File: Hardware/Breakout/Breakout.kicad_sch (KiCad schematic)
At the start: 1 part, among them IC1 NUCLEO-G431KB

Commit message: Added few parts
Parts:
- added U1: TDC7200PWR, SOP65P640X120-14N, symbol TDC7200PWR:TDC7200PWR
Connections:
- net GND1: now also U1.7 (GND)
- net at IC1.13 (PA11(D10)): now also U1.11 (~{CS})
- net at IC1.14 (PB5(D11)): now also U1.9 (DOUT)
- net at IC1.15 (PB4(D12)): now also U1.10 (DIN)
- net at IC1.16 (PB3(D13)): now also U1.12 (SCLK)
- net at IC1.17 (+3V3): now also U1.14 (VDD)
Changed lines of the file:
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@@
+    (stroke (width 0) (type default))
+  )
+  (wire (pts (xy 66.04 101.6) (xy 66.04 116.84))
+    (stroke (width 0) (type default))
+  )
+  (wire (pts (xy 116.84 106.68) (xy 134.62 106.68))
+    (stroke (width 0) (type default))
+  )
+  (wire (pts (xy 147.32 116.84) (xy 147.32 106.68))
+    (stroke (width 0) (type default))
+  )
+  (wire (pts (xy 134.62 109.22) (xy 163.83 109.22))
+    (stroke (width 0) (type default))
+  )
+  (wire (pts (xy 134.62 106.68) (xy 134.62 109.22))
     (stroke (width 0) (type default))
   )
@@
     (stroke (width 0) (type default))
   )
+  (wire (pts (xy 68.58 104.14) (xy 68.58 114.3))
+    (stroke (width 0) (type default))
+  )
+  (wire (pts (xy 68.58 114.3) (xy 163.83 114.3))
+    (stroke (width 0) (type default))
+  )
   (wire (pts (xy 116.84 71.12) (xy 121.92 71.12))
     (stroke (width 0) (type default))
   )
+  (wire (pts (xy 71.12 101.6) (xy 66.04 101.6))
+    (stroke (width 0) (type default))
+  )
+  (wire (pts (xy 147.32 106.68) (xy 163.83 106.68))
+    (stroke (width 0) (type default))
+  )
+  (wire (pts (xy 139.7 86.36) (xy 163.83 86.36))
+    (stroke (width 0) (type default))
+  )
+  (wire (pts (xy 71.12 111.76) (xy 163.83 111.76))
+    (stroke (width 0) (type default))
+  )
+  (wire (pts (xy 116.84 104.14) (xy 139.7 104.14))
+    (stroke (width 0) (type default))
+  )
+  (wire (pts (xy 139.7 104.14) (xy 139.7 86.36))
+    (stroke (width 0) (type default))
+  )
+  (wire (pts (xy 66.04 116.84) (xy 147.32 116.84))
+    (stroke (width 0) (type default))
+  )
+  (wire (pts (xy 71.12 106.68) (xy 71.12 111.76))
+    (stroke (width 0) (type default))
+  )
   (wire (pts (xy 127 73.66) (xy 116.84 73.66))
     (stroke (width 0) (type default))
   )
+  (wire (pts (xy 199.39 121.92) (xy 203.2 121.92))
+    (stroke (width 0) (type default))
+  )
+  (wire (pts (xy 203.2 121.92) (xy 203.2 127))
+    (stroke (width 0) (type default))
+  )
+  (wire (pts (xy 71.12 104.14) (xy 68.58 104.14))
+    (stroke (width 0) (type default))
+  )
   (symbol (lib_id "power:GND1") (at 127 63.5 180) (unit 1)
     (in_bom yes) (on_board yes) (dnp no) (fields_autoplaced)
@@
         (path "/c2ef38f9-0f55-4b19-9130-d81b036a0cd1"
           (reference "#PWR01") (unit 1)
+        )
+      )
+    )
+  )
+  (symbol (lib_id "power:GND1") (at 203.2 127 0) (unit 1)
+    (in_bom yes) (on_board yes) (dnp no) (fields_autoplaced)
+    (property "Reference" "#PWR03" (at 203.2 133.35 0)
+      (effects (font (size 1.27 1.27)) hide)
+    )
+    (property "Value" "GND1" (at 203.2 132.08 0)
+      (effects (font (size 1.27 1.27)))
+    )
+    (property "Footprint" "" (at 203.2 127 0)
+      (effects (font (size 1.27 1.27)) hide)
+    )
+    (property "Datasheet" "" (at 203.2 127 0)
+      (effects (font (size 1.27 1.27)) hide)
+    )
+    (pin "1")
+    (instances
+      (project "Breakout"
+        (path "/c2ef38f9-0f55-4b19-9130-d81b036a0cd1"
+          (reference "#PWR03") (unit 1)
         )
       )
@@
         )
       )
+    )
+  )
+  (symbol (lib_id "TDC7200PWR:TDC7200PWR") (at 181.61 104.14 0) (unit 1)
+    (in_bom yes) (on_board yes) (dnp no) (fields_autoplaced)
+    (property "Reference" "U1" (at 181.61 78.74 0)
+      (effects (font (size 1.27 1.27)))
+    )
+    (property "Value" "TDC7200PWR" (at 181.61 81.28 0)
+      (effects (font (size 1.27 1.27)))
+    )
+    (property "Footprint" "SOP65P640X120-14N" (at 181.61 104.14 0)
+      (effects (font (size 1.27 1.27)) (justify bottom) hide)
+    )
+    (property "Datasheet" "" (at 181.61 104.14 0)
+      (effects (font (size 1.27 1.27)) hide)
+    )
+    (property "PARTREV" "D" (at 181.61 104.14 0)
+      (effects (font (size 1.27 1.27)) (justify bottom) hide)
+    )
+    (property "MANUFACTURER" "Texas Instruments" (at 181.61 104.14 0)
+      (effects (font (size 1.27 1.27)) (justify bottom) hide)
+    )
+    (property "MAXIMUM_PACKAGE_HEIGHT" "1.2 mm" (at 181.61 104.14 0)
+      (effects (font (size 1.27 1.27)) (justify bottom) hide)
+    )
+    (property "STANDARD" "IPC 7351B" (at 181.61 104.14 0)
+      (effects (font (size 1.27 1.27)) (justify bottom) hide)
+    )
+    (pin "1")
+    (pin "10")
+    (pin "11")
+    (pin "12")
+    (pin "13")
+    (pin "14")
+    (pin "2")
+    (pin "3")
+    (pin "4")
+    (pin "5")
+    (pin "6")
+    (pin "7")
+    (pin "8")
+    (pin "9")
+    (instances
+      (project "Breakout"
+        (path "/c2ef38f9-0f55-4b19-9130-d81b036a0cd1"
+          (reference "U1") (unit 1)
+        )
+      )

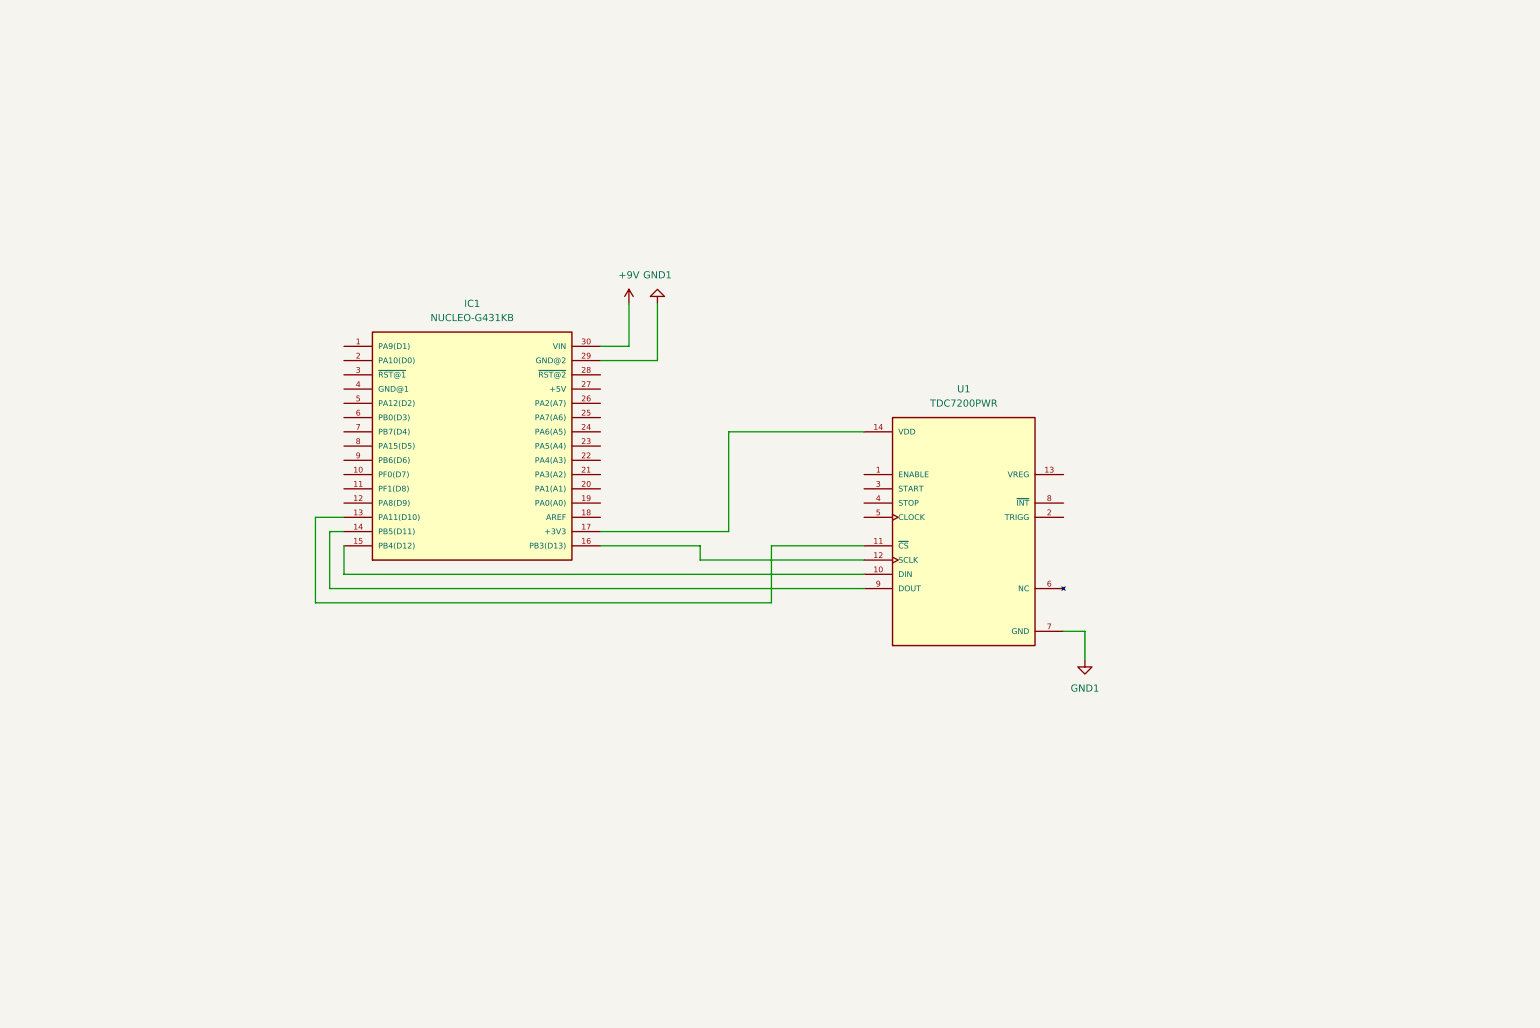
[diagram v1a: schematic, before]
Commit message: Added TDC circiut to main schem, still need to make sure its all hoodked up right
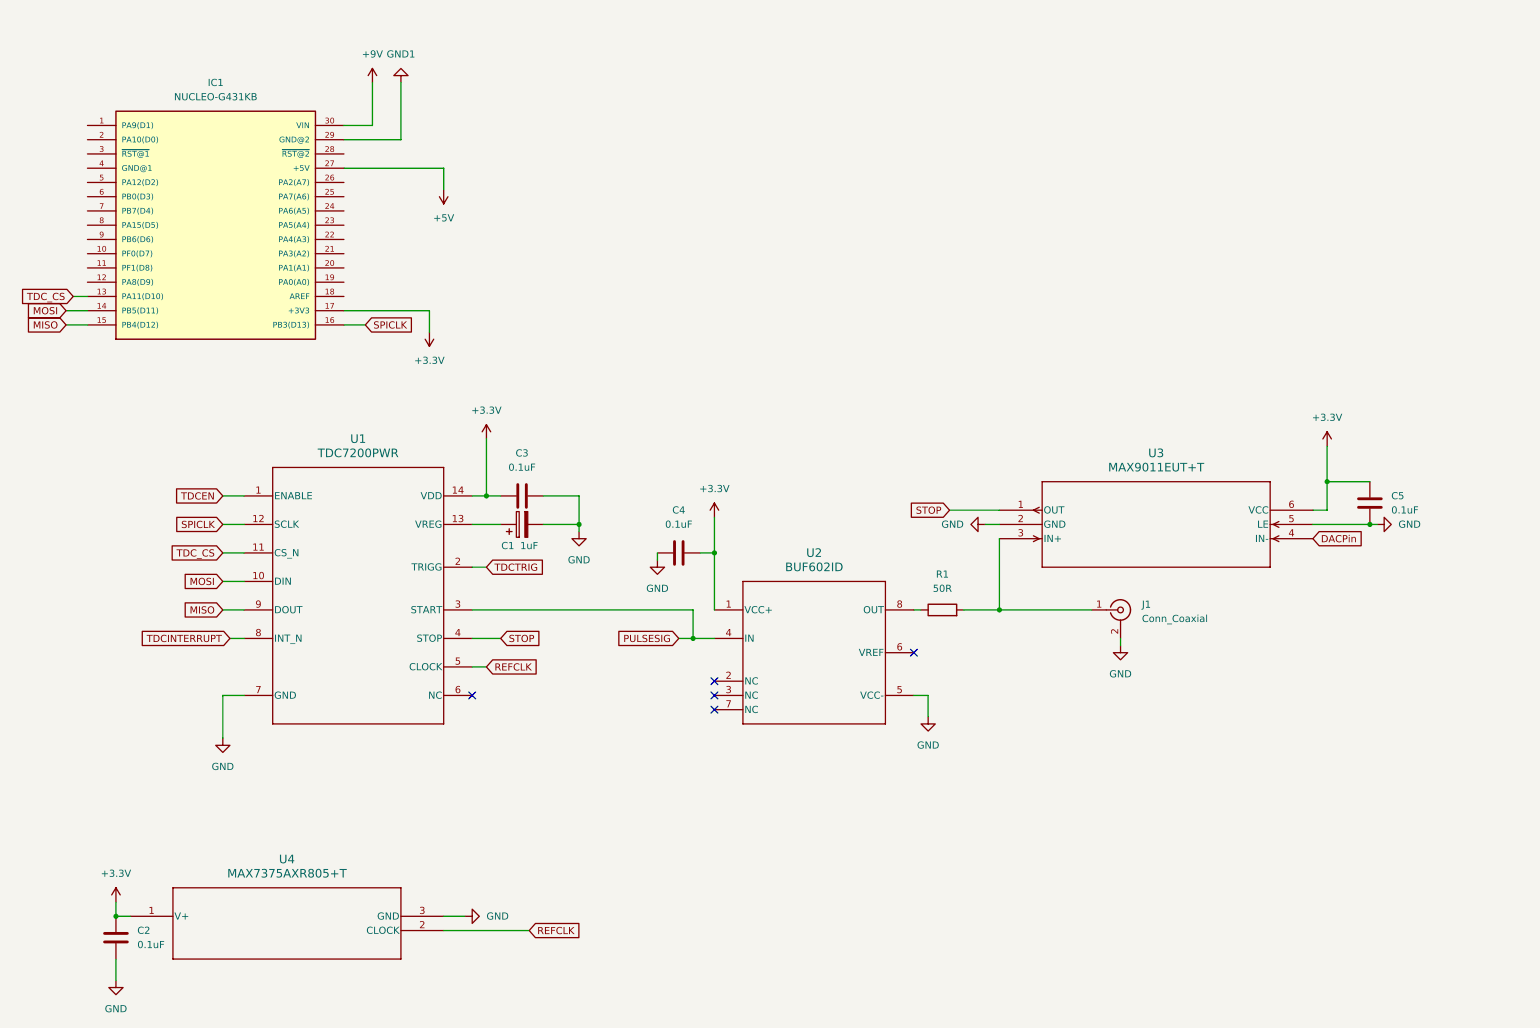
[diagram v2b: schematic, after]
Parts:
- removed U1: TDC7200PWR, SOP65P640X120-14N, symbol TDC7200PWR:TDC7200PWR
- added C1: 1uF, symbol Device:C_Polarized
- added C2, C3, C4, C5: 0.1uF, symbol Device:C
- added J1: Conn_Coaxial, symbol Connector:Conn_Coaxial
- added R1: 50R, symbol Device:R
- added U1: TDC7200PWR, PW0014A_N, symbol TDC:TDC7200PWR
- added U2: BUF602ID, D0008A_N, symbol 2023-07-05_03-38-51:BUF602ID
- added U3: MAX9011EUT+T, 21-0058I_MXM, symbol 2023-07-05_03-30-52:MAX9011EUT+T
- added U4: MAX7375AXR805+T, 21-0075D_MXM, symbol 2023-07-05_04-24-47:MAX7375AXR805+T
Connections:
- net TDC_CS: now reaches IC1.13 (PA11(D10))
- net TDC_CS: now also U1.11 (CS_N)
- net MOSI: now reaches IC1.14 (PB5(D11))
- net MOSI: now also U1.10 (DIN)
- net MISO: now reaches IC1.15 (PB4(D12))
- net MISO: now also U1.9 (DOUT)
- net SPICLK: now reaches IC1.16 (PB3(D13))
- net SPICLK: now also U1.12 (SCLK)
- net +3.3V: now reaches IC1.17 (+3V3)
- net +3.3V: now also C2.1, C3.1, C4.2, C5.2, U1.14 (VDD), U2.1 (VCC+), U3.6 (VCC), U4.1 (V+)
- net +5V: now reaches IC1.27 (+5V)
- new net: J1.1 (In), R1.2, U3.3 (IN+)
- new net: R1.1, U2.8 (OUT)
- new net: C1.1, U1.13 (VREG)
- new net DACPin: U3.4 (IN-)
- new net GND: C1.2, C2.2, C3.2, C4.1, C5.1, J1.2 (Ext), U1.7 (GND), U2.5 (VCC-), U3.2 (GND), U3.5 (LE), U4.3 (GND)
- new net PULSESIG: U1.3 (START), U2.4 (IN)
- new net REFCLK: U1.5 (CLOCK), U4.2 (CLOCK)
- new net STOP: U1.4 (STOP), U3.1 (OUT)
- new net TDCEN: U1.1 (ENABLE)
- new net TDCINTERRUPT: U1.8 (INT_N)
- new net TDCTRIG: U1.2 (TRIGG)
- no-connect marks 0 -> 5
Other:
- moved on the sheet: IC1

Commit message: Upload of hardware changes as of 6pm 06/07/2023
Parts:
- added B2: SSD1306, Library:Adafruit_SSD1306_4Pin, symbol SSD1306-128x64_OLED:SSD1306
- B1: renamed from IC1; footprint (none) -> NUCLEO-G431KB:DIPS1524W66P254L5029H1500Q30N
- C1: footprint (none) -> UWT1HH010MCL1GB:PCAP_4x5.4-ELECT_NCA-L
- C2, C3, C4, C5: footprint (none) -> 06035C104JAT2A:CAPC1608X90N
- J1: footprint (none) -> Library:0731375003_BCN_conn
- U1: footprint PW0014A_N -> TDC7200PWR:SOP65P640X120-14N
- U2: footprint D0008A_N -> BUF602ID:D0008A_N
- U3: footprint 21-0058I_MXM -> MAX9011EUT:21-0058I_MXM
- U4: footprint 21-0075D_MXM -> MAX737AXR805:21-0075D_MXM
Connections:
- net GND1 is gone; now on net GND: B1.29 (GND@2)
- net +3.3V: now also B2.2 (VCC)
- net DACPin: now also B1.26 (PA2(A7))
- net GND: now also B1.4 (GND@1), B2.1 (GND)
- net PULSESIG: now also B1.6 (PB0(D3))
- net TDCEN: now also B1.9 (PB6(D6))
- net TDCINTERRUPT: now also B1.12 (PA8(D9))
- net TDCTRIG: now also B1.10 (PF0(D7))
- net SDA: now reaches B1.7 (PB7(D4))
- net SDA: now also B2.4 (SDA)
- net SCL: now reaches B1.8 (PA15(D5))
- net SCL: now also B2.3 (SCL)
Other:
- moved on the sheet: B1

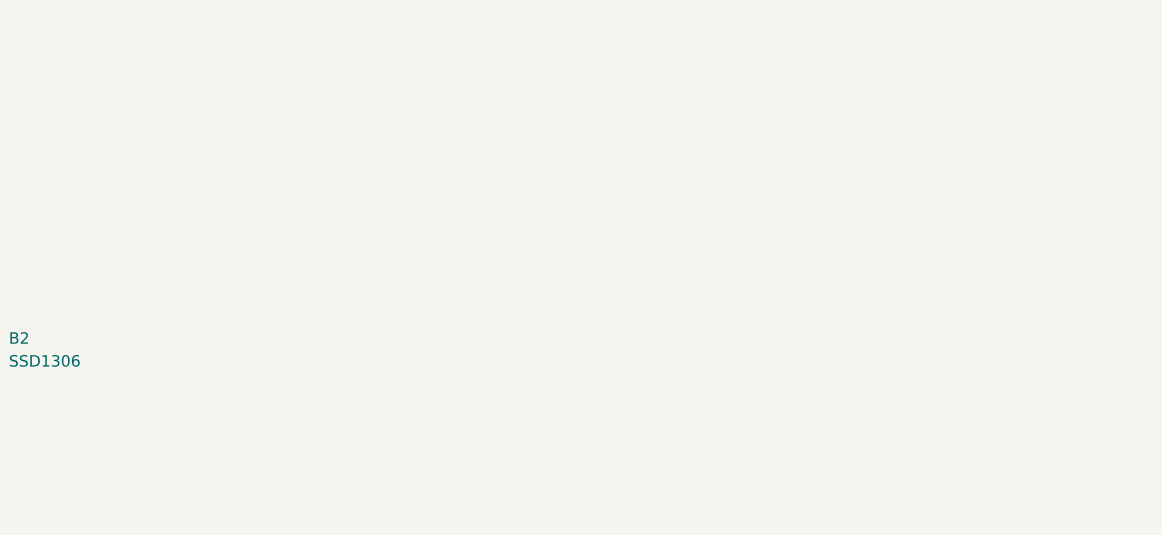
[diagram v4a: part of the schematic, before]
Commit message: Buttons and fine turning still required
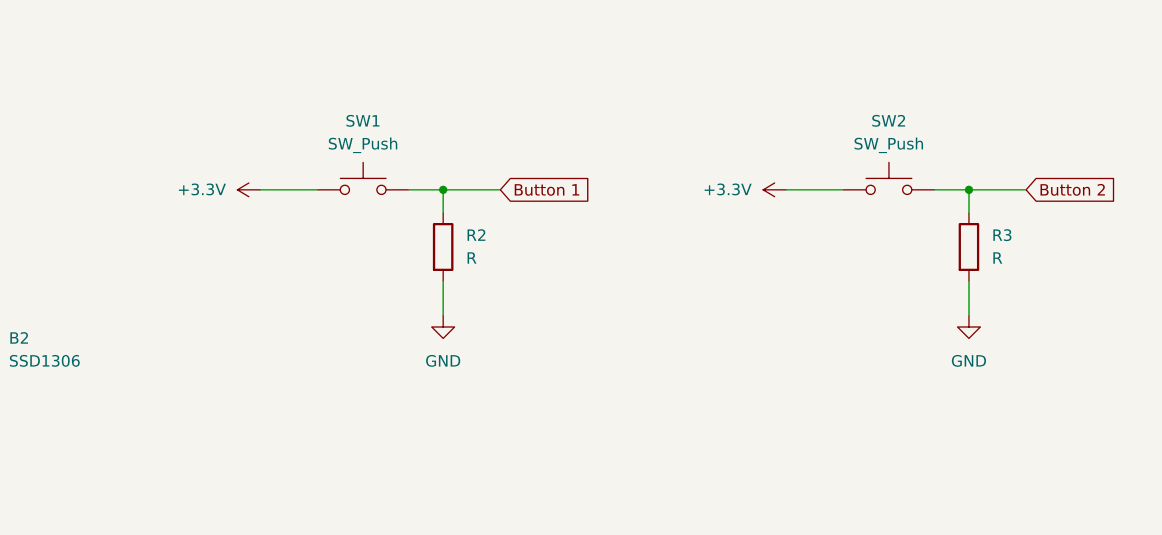
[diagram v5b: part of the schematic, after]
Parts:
- added R2, R3: R, symbol Device:R
- added SW1, SW2: SW_Push, symbol Switch:SW_Push
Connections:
- net +3.3V: now also SW1.1, SW2.1
- net GND: now also R2.2, R3.2
- new net Button 1: R2.1, SW1.2
- new net Button 2: R3.1, SW2.2

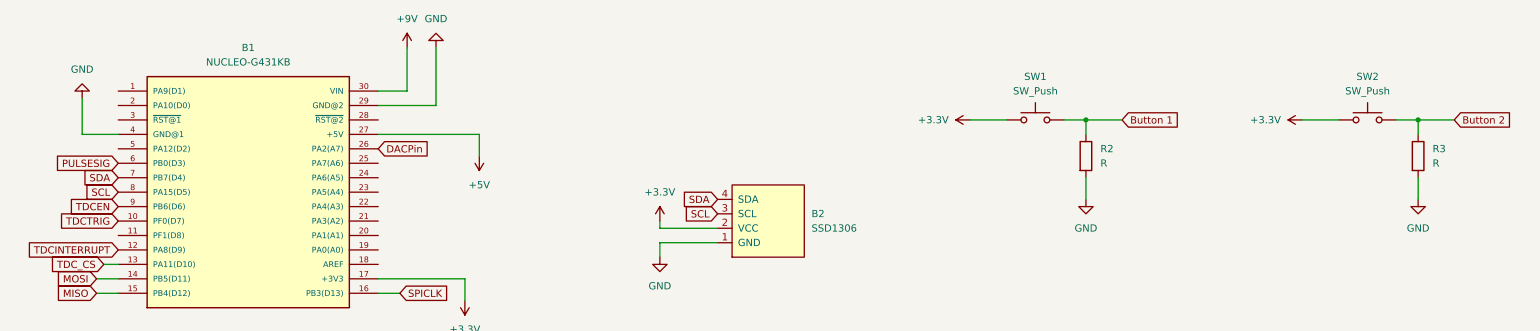
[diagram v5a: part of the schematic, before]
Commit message: Almost final board, need to fix silkscreen
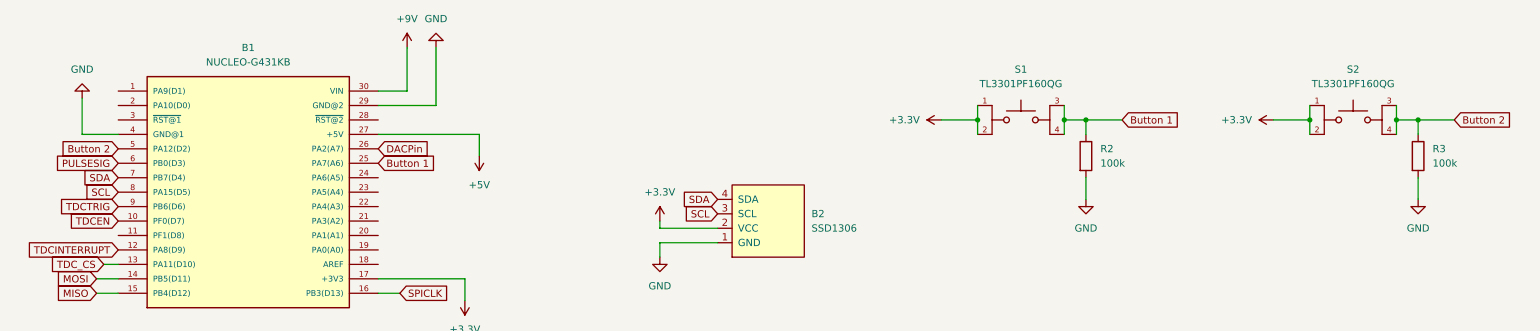
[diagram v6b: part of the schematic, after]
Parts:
- removed SW1, SW2: SW_Push, symbol Switch:SW_Push
- added S1, S2: TL3301PF160QG, TL3301PF160QG:SW_TL3301PF160QG, symbol TL3301PF160QG:TL3301PF160QG
- R1: footprint (none) -> WSC251550R00FEA:RES_WSC_2515-M
- R2, R3: value R -> 100k; footprint (none) -> CRCW0201100KFKED:RC0201N_VIS-M
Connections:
- net +3.3V: now also S1.1, S1.2, S2.1, S2.2
- net Button 1: now also B1.25 (PA7(A6)), S1.3, S1.4
- net Button 2: now also B1.5 (PA12(D2)), S2.3, S2.4
- net TDCEN: now also B1.10 (PF0(D7)); no longer B1.9 (PB6(D6))
- net TDCTRIG: now also B1.9 (PB6(D6)); no longer B1.10 (PF0(D7))
